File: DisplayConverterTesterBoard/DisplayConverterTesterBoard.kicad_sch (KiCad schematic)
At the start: 2 parts, among them J3 Conn_01x03

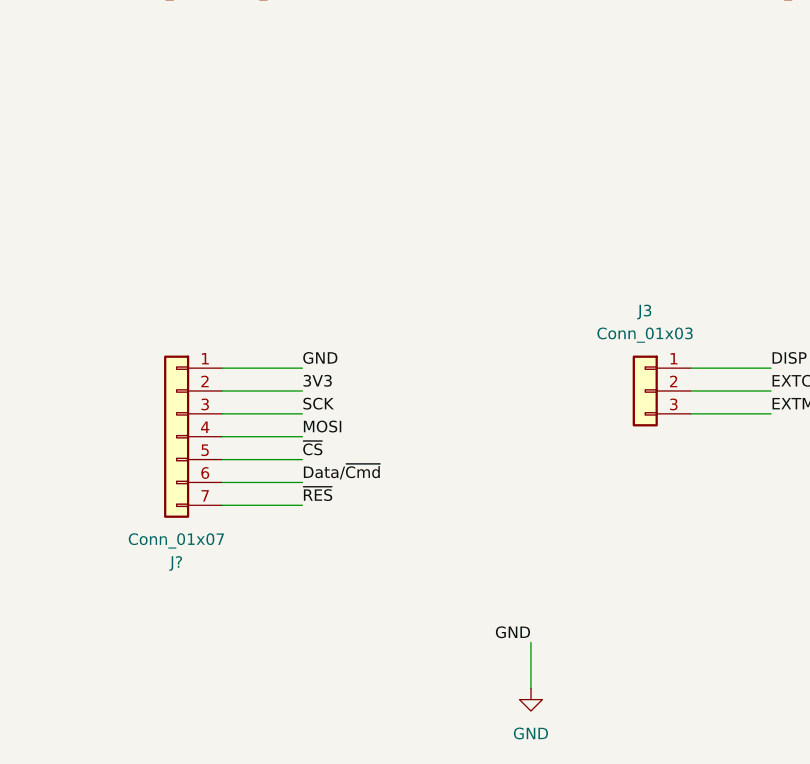
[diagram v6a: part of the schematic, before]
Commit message: fix ERCs
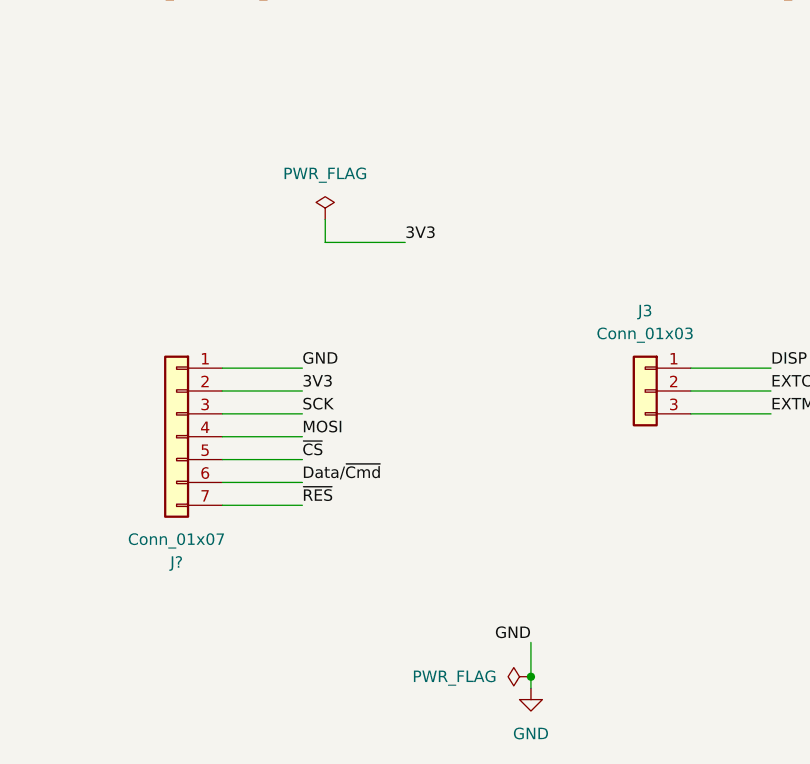
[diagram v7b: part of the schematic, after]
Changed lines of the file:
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@@
 (kicad_sch (version 20230121) (generator eeschema)
   (paper "A4")
+  (junction (at 102.87 165.1) (diameter 0) (color 0 0 0 0)
+  )
   (wire (pts (xy 68.58 138.43) (xy 77.47 138.43))
     (stroke (width 0) (type default))
@@
     (stroke (width 0) (type default))
   )
+  (wire (pts (xy 102.87 165.1) (xy 102.87 166.37))
+    (stroke (width 0) (type default))
+  )
   (wire (pts (xy 124.46 63.5) (xy 115.57 63.5))
     (stroke (width 0) (type default))
@@
     (stroke (width 0) (type default))
   )
+  (wire (pts (xy 80.01 116.84) (xy 88.9 116.84))
+    (stroke (width 0) (type default))
+  )
   (wire (pts (xy 53.34 66.04) (xy 44.45 66.04))
     (stroke (width 0) (type default))
@@
     (stroke (width 0) (type default))
   )
-  (wire (pts (xy 102.87 161.29) (xy 102.87 166.37))
+  (wire (pts (xy 102.87 161.29) (xy 102.87 165.1))
+    (stroke (width 0) (type default))
+  )
+  (wire (pts (xy 80.01 114.3) (xy 80.01 116.84))
     (stroke (width 0) (type default))
   )
@@
     (effects (font (size 1.27 1.27)) (justify right bottom))
   )
+  (label "3V3" (at 88.9 116.84 0) (fields_autoplaced)
+    (effects (font (size 1.27 1.27)) (justify left bottom))
+  )
   (label "3V3" (at 44.45 55.88 180) (fields_autoplaced)
     (effects (font (size 1.27 1.27)) (justify right bottom))
@@
     (effects (font (size 1.27 1.27)) (justify left bottom))
   )
+  (symbol (lib_id "power:PWR_FLAG") (at 102.87 165.1 90) (unit 1)
+    (in_bom yes) (on_board yes) (dnp no) (fields_autoplaced)
+    (property "Reference" "#FLG0102" (at 100.965 165.1 0)
+      (effects (font (size 1.27 1.27)) hide)
+    )
+    (property "Value" "PWR_FLAG" (at 99.06 165.1 90)
+      (effects (font (size 1.27 1.27)) (justify left))
+    )
+    (property "Footprint" "" (at 102.87 165.1 0)
+      (effects (font (size 1.27 1.27)) hide)
+    )
+    (property "Datasheet" "~" (at 102.87 165.1 0)
+      (effects (font (size 1.27 1.27)) hide)
+    )
+    (pin "1")
+    (instances
+      (project "DisplayConverterTesterBoard"
+        (path "/58d9d6aa-d5e3-4b7b-b546-d57c329de758"
+          (reference "#FLG0102") (unit 1)
+        )
+      )
+    )
+  )
+  (symbol (lib_id "power:PWR_FLAG") (at 80.01 114.3 0) (unit 1)
+    (in_bom yes) (on_board yes) (dnp no) (fields_autoplaced)
+    (property "Reference" "#FLG0101" (at 80.01 112.395 0)
+      (effects (font (size 1.27 1.27)) hide)
+    )
+    (property "Value" "PWR_FLAG" (at 80.01 109.22 0)
+      (effects (font (size 1.27 1.27)))
+    )
+    (property "Footprint" "" (at 80.01 114.3 0)
+      (effects (font (size 1.27 1.27)) hide)
+    )
+    (property "Datasheet" "~" (at 80.01 114.3 0)
+      (effects (font (size 1.27 1.27)) hide)
+    )
+    (pin "1")
+    (instances
+      (project "DisplayConverterTesterBoard"
+        (path "/58d9d6aa-d5e3-4b7b-b546-d57c329de758"
+          (reference "#FLG0101") (unit 1)
+        )
+      )
+    )
+  )
   (symbol (lib_id "power:GND") (at 102.87 166.37 0) (unit 1)
